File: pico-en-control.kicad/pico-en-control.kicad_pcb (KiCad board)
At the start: 2 copper layers, 17 parts, among them J1 JST-PH2 Bat, J2 Pico Pin 1-7, J3 Pico Pin 40-34, SW1 SW_Push, U1 SN74HC74N, U2 PCF8563T, Y1 Crystal

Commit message: draft routing
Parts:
- moved D1 15.8 mm to (103.3, 104.5)
- moved R1 14.7 mm to (115.7, 115.7), turned to 90 degrees
- moved SW1 14.2 mm to (113.5, 130.7), turned to 90 degrees
- moved J1 14.1 mm to (106.4, 126.9)
- moved C1 11.6 mm to (106.4, 111.4), turned to 0 degrees
- moved U1 11.1 mm to (109.7, 115.7), turned to 90 degrees
- moved JP1 9.63 mm to (115.2, 112.1), turned to 90 degrees
- moved R5 9.61 mm to (111.4, 109.9), turned to -90 degrees
- moved C3 8.32 mm to (114.1, 102.3), turned to 90 degrees
- moved Y1 8.27 mm to (111.9, 100.1), turned to 180 degrees
- moved C2 8.23 mm to (114.0, 107.9), turned to 90 degrees
- moved R4 6.82 mm to (108.0, 110.0), turned to -90 degrees
- moved R2 6.41 mm to (105.8, 120.5), turned to -90 degrees
- moved R3 6.15 mm to (110.1, 109.9)
- moved U2 2.48 mm to (110.7, 105.1), turned to -90 degrees
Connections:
- J2 pad 2: /GP2 -> unconnected-(J2-Pad2)
- J2 pad 6: /GP4_DONE -> /GP4_CLKOUT
- J2 pad 7: unconnected-(J2-Pad7) -> /GP5_DONE
- JP1 pad 1: /GP2 -> /GP4_CLKOUT
- R1 pad 2: /GP4_DONE -> /GP5_DONE
- R5 pad 1: +BATT -> /CLKOUT
- R5 pad 2: /CLKOUT -> +3V3
- U1 pad 3: /GP4_DONE -> /GP5_DONE
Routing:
- net +BATT: track 0.00 -> 50.6 mm, vias 0 -> 2
- net /1~{PRE}: track 0.00 -> 50.0 mm, vias 0 -> 3
- net /3V3_EN: track 0.00 -> 24.5 mm, vias 0 -> 1
- net /GP5_DONE: track 0.00 -> 13.2 mm, vias 0 -> 1
- net +3V3: track 0.00 -> 12.4 mm, vias 0 -> 1
- net /SDA: track 0.00 -> 12.2 mm, vias 0 -> 1
- net /SCL: track 0.00 -> 12.1 mm, vias 0 -> 1
- net Net-(U1-Pad2): track 0.00 -> 9.89 mm
- net /CLKOUT: track 0.00 -> 6.74 mm, vias 0 -> 1
- net Net-(C3-Pad2): track 0.00 -> 4.57 mm
- net /VSYS: track 0.00 -> 2.98 mm
- net Net-(U2-Pad2): track 0.00 -> 2.80 mm
- net /GP4_CLKOUT: track 0.00 -> 2.27 mm
- net GND: vias 0 -> 1
- added copper zone on B.Cu, net GND
- added copper zone on F.Cu, net GND
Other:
- board outline added: 21 x 33.8 mm

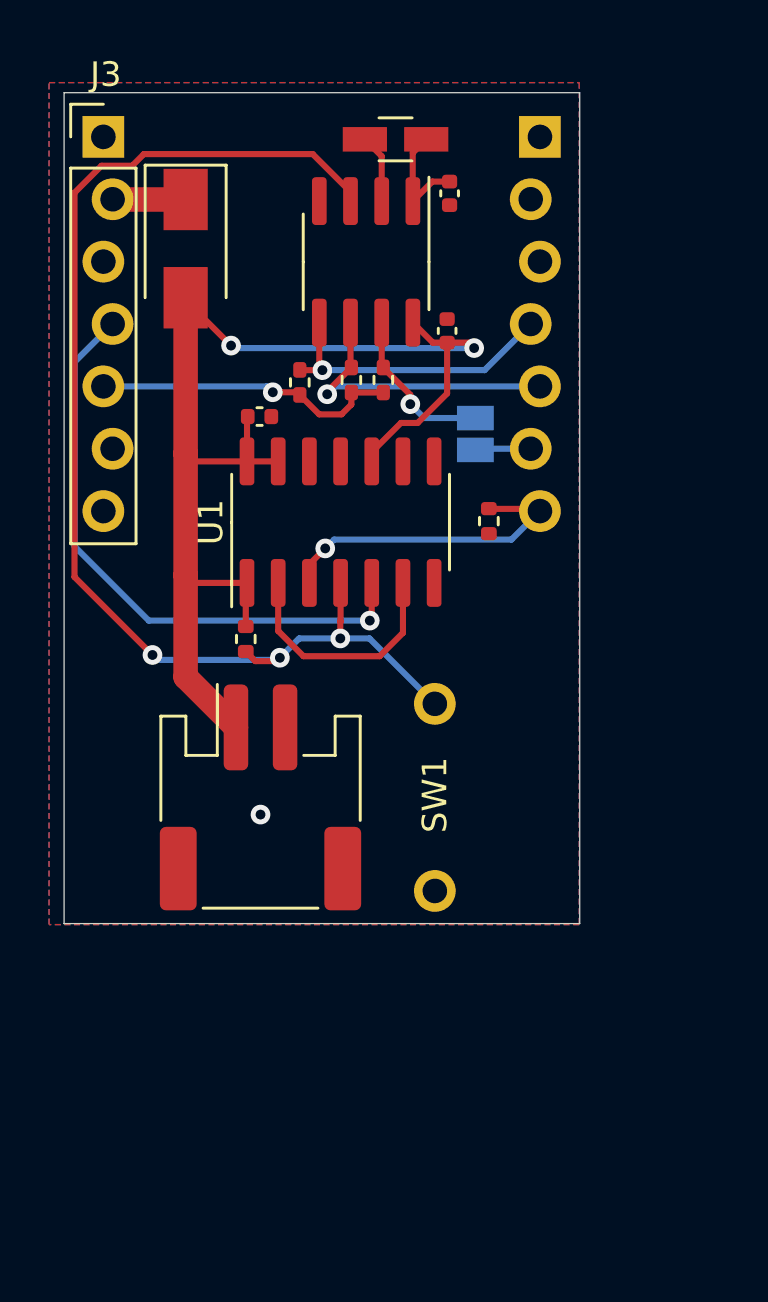
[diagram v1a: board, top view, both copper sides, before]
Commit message: switched to 13-pin connectors
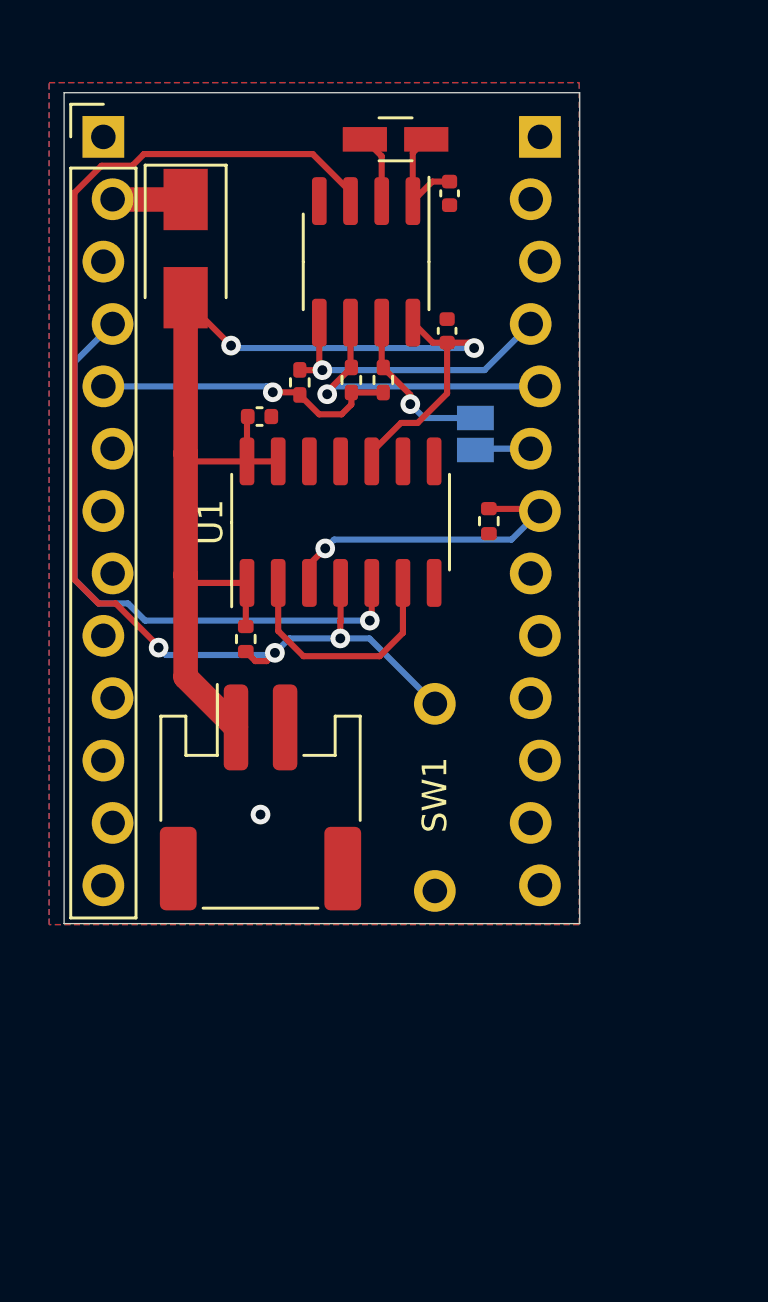
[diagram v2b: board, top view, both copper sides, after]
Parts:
- J2: value Pico Pin 1-7 -> Pico Pin 1-13; footprint user:Connector_1x7_no_solder -> user:Connector_1x13_no_solder; moved to B.Cu
- J3: value Pico Pin 40-34 -> Pico Pin 40-28; footprint user:Connector_1x7_no_solder -> user:Connector_1x13_no_solder
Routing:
- net /3V3_EN: track 24.5 -> 25.3 mm

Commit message: DRC ok
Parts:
- moved C1 2.67 mm to (104.5, 113.3), turned to -90 degrees
- moved R3 0.50 mm to (110.1, 110.4)
- moved R4 0.50 mm to (108.0, 110.5)
- moved R5 0.50 mm to (111.4, 110.4)
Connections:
- J2 pad 13: unconnected-(J2-Pad13) -> GND
- J2 pad 8: unconnected-(J2-Pad8) -> GND
- J3 pad 13: unconnected-(J3-Pad13) -> GND
- J3 pad 8: unconnected-(J3-Pad8) -> GND
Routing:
- net GND: track 0.00 -> 27.7 mm, vias 1 -> 5
- net /SDA: track 12.2 -> 13.0 mm
- net /SCL: track 12.1 -> 12.7 mm

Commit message: Rev2
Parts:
- SW1: value SW_Push -> SW_Push_SLIM
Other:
- board text added: "GND"
- board text added: "GP4_CLKOUT"
- board text added: "GP5_DONE"
- board text added: "On"
- board text added: "SCL"
- board text added: "SDA"
- board text added: "github.com/bablokb/pico-en-control Rev. 2"
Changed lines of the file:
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@@
     )
-  )
-  (footprint "user:SW_PUSH_SLIM_1x4" (layer "F.Cu")
-    (at 113.5 130.71 90)
-    (descr "Prototyping Area")
-    (tags "connector")
-    (property "Sheetfile" "pico-en-control.kicad_sch")
-    (property "Sheetname" "")
-    (attr exclude_from_pos_files)
-    (fp_text reference "SW1" (at 3.91 0 90) (layer "F.SilkS")
-      (effects (font (size 1 1) (thickness 0.15)))
-    )
-    (fp_text value "SW_Push" (at 3.73126 2.92608 90) (layer "F.Fab")
-      (effects (font (size 1 1) (thickness 0.15)))
-    )
-    (fp_text user "${REFERENCE}" (at 1.27 1.27 90) (layer "F.Fab")
-      (effects (font (size 1 1) (thickness 0.15)))
-    )
-    (fp_line (start -1.27 -1.8) (end -1.27 1.8) (layer "F.CrtYd") (width 0.05))
-    (fp_line (start 8.89 -1.8) (end 8.89 1.8) (layer "F.CrtYd") (width 0.05))
-    (fp_line (start -1.27 1.8) (end 8.89 1.8) (layer "F.CrtYd") (width 0.05))
-    (fp_line (start -1.27 -1.8) (end 8.89 -1.8) (layer "F.CrtYd") (width 0.05))
-    (pad "1" thru_hole circle locked (at 0 0 90) (size 1.7 1.7) (drill 1) (layers *.Cu *.Mask)
-      (net 2 "GND") (pinfunction "1") (pintype "passive"))
-    (pad "2" thru_hole circle locked (at 7.62 0 90) (size 1.7 1.7) (drill 1) (layers *.Cu *.Mask)
-      (net 17 "/1~{PRE}") (pinfunction "2") (pintype "passive"))
   )
   (footprint "Crystal:Crystal_SMD_3215-2Pin_3.2x1.5mm" (layer "F.Cu")
@@
     (property "Status" "Active")
     (attr smd)
-    (fp_text reference "U1" (at 0 -5.28 90) (layer "F.SilkS")
+    (fp_text reference "U1" (at 0 -5.28 90) (layer "F.SilkS") hide
       (effects (font (size 1 1) (thickness 0.15)))
     )
@@
     )
   )
+  (footprint "user:SW_PUSH_SLIM_1x4" (layer "F.Cu")
+    (at 113.5 130.7 90)
+    (descr "Slim Pushbutton")
+    (tags "connector")
+    (property "Sheetfile" "pico-en-control.kicad_sch")
+    (property "Sheetname" "")
+    (attr exclude_from_pos_files exclude_from_bom)
+    (fp_text reference "SW1" (at 2.7 0 180) (layer "F.SilkS") hide
+      (effects (font (size 1 1) (thickness 0.15)))
+    )
+    (fp_text value "SW_Push_SLIM" (at 3.73126 2.92608 90) (layer "F.Fab")
+      (effects (font (size 1 1) (thickness 0.15)))
+    )
+    (fp_text user "${REFERENCE}" (at 1.27 1.27 90) (layer "F.Fab")
+      (effects (font (size 1 1) (thickness 0.15)))
+    )
+    (fp_line (start -1.27 1.8) (end 8.89 1.8) (layer "F.CrtYd") (width 0.05))
+    (fp_line (start -1.27 -1.8) (end 8.89 -1.8) (layer "F.CrtYd") (width 0.05))
+    (fp_line (start 8.89 -1.8) (end 8.89 1.8) (layer "F.CrtYd") (width 0.05))
+    (fp_line (start -1.27 -1.8) (end -1.27 1.8) (layer "F.CrtYd") (width 0.05))
+    (pad "1" thru_hole circle (at 0 0 90) (size 1.7 1.7) (drill 1) (layers *.Cu *.Mask)
+      (net 2 "GND") (pinfunction "1") (pintype "passive"))
+    (pad "2" thru_hole circle (at 7.62 0 90) (size 1.7 1.7) (drill 1) (layers *.Cu *.Mask)
+      (net 17 "/1~{PRE}") (pinfunction "2") (pintype "passive"))
+    (pad "3" thru_hole circle (at 5.08 0 90) (size 1.7 1.7) (drill 1) (layers *.Cu *.Mask)
+      (net 2 "GND") (pinfunction "1") (pintype "passive"))
+  )
   (footprint "Resistor_SMD:R_0402_1005Metric" (layer "F.Cu")
     (at 111.4 110.4 -90)
@@
     (property "Sheetfile" "pico-en-control.kicad_sch")
     (property "Sheetname" "")
-    (attr through_hole)
+    (attr through_hole exclude_from_pos_files exclude_from_bom)
     (fp_text reference "J3" (at 0.1 -2.54) (layer "F.SilkS") hide
       (effects (font (size 1 1) (thickness 0.15)))
@@
     (property "Sheetfile" "pico-en-control.kicad_sch")
     (property "Sheetname" "")
-    (attr smd)
+    (attr smd exclude_from_pos_files exclude_from_bom)
     (fp_text reference "J1" (at 0 -5.8) (layer "F.SilkS") hide
       (effects (font (size 1 1) (thickness 0.15)))
@@
     (pad "2" smd roundrect (at 1 -2.85) (size 1 3.5) (layers "F.Cu" "F.Paste" "F.Mask") (roundrect_rratio 0.25)
       (net 2 "GND") (pinfunction "Pin_2") (pintype "passive"))
-    (pad "MP" smd roundrect (at -3.35 2.9) (size 1.5 3.4) (layers "F.Cu" "F.Paste" "F.Mask") (roundrect_rratio 0.166667))
-    (pad "MP" smd roundrect (at 3.35 2.9) (size 1.5 3.4) (layers "F.Cu" "F.Paste" "F.Mask") (roundrect_rratio 0.166667))
+    (pad "MP" smd roundrect (at -3.35 2.9) (size 1.5 3.4) (layers "F.Cu" "F.Paste" "F.Mask") (roundrect_rratio 0.1666673333))
+    (pad "MP" smd roundrect (at 3.35 2.9) (size 1.5 3.4) (layers "F.Cu" "F.Paste" "F.Mask") (roundrect_rratio 0.1666673333))
     (model "${KICAD6_3DMODEL_DIR}/Connector_JST.3dshapes/JST_PH_S2B-PH-SM4-TB_1x02-1MP_P2.00mm_Horizontal.wrl"
       (offset (xyz 0 0 0))
@@
     (property "Sheetfile" "pico-en-control.kicad_sch")
     (property "Sheetname" "")
-    (attr through_hole)
+    (attr through_hole exclude_from_pos_files exclude_from_bom)
     (fp_text reference "J2" (at 0.1 2.54) (layer "B.SilkS") hide
       (effects (font (size 1 1) (thickness 0.15)) (justify mirror))
@@
     (property "Sheetfile" "pico-en-control.kicad_sch")
     (property "Sheetname" "")
-    (attr exclude_from_pos_files)
+    (attr exclude_from_pos_files exclude_from_bom)
     (fp_text reference "JP1" (at 0 1.8 90) (layer "B.SilkS") hide
       (effects (font (size 1 1) (thickness 0.15)) (justify mirror))
@@
       (net 16 "/CLKOUT") (pinfunction "B") (pintype "passive"))
   )
+  (gr_circle (center 104.723607 118.1) (end 104.947214 118.1) (layer "F.SilkS") (width 0.12) (fill solid))
+  (gr_circle (center 114.1 103.6) (end 114.323607 103.6) (layer "F.SilkS") (width 0.12) (fill solid))
   (gr_rect (start 98.4 98.2) (end 119.4 132.04) (layer "Edge.Cuts") (width 0.05) (fill none))
+  (gr_text "GP4_CLKOUT" (at 109.2 112.9) (layer "B.SilkS")
+    (effects (font (size 1 1) (thickness 0.15)) (justify mirror))
+  )
+  (gr_text "GND" (at 112.3 130.8) (layer "B.SilkS")
+    (effects (font (size 1 1) (thickness 0.15)) (justify left mirror))
+  )
+  (gr_text "GND" (at 104.7 130.6) (layer "B.SilkS")
+    (effects (font (size 1 1) (thickness 0.15)) (justify left mirror))
+  )
+  (gr_text "SCL" (at 116.4 109.8) (layer "B.SilkS")
+    (effects (font (size 1 1) (thickness 0.15)) (justify left mirror))
+  )
+  (gr_text "github.com/bablokb/pico-en-control\nRev. 2" (at 103.2 98.5 90) (layer "B.SilkS")
+    (effects (font (size 1 1) (thickness 0.15)) (justify left mirror))
+  )
+  (gr_text "GND" (at 112.4 125.7) (layer "B.SilkS")
+    (effects (font (size 1 1) (thickness 0.15)) (justify left mirror))
+  )
+  (gr_text "SDA" (at 116.3 107.6) (layer "B.SilkS")
+    (effects (font (size 1 1) (thickness 0.15)) (justify left mirror))
+  )
+  (gr_text "GND" (at 116.2 105.2) (layer "B.SilkS")
+    (effects (font (size 1 1) (thickness 0.15)) (justify left mirror))
+  )
+  (gr_text "GP5_DONE" (at 112.5 115.3) (layer "B.SilkS")
+    (effects (font (size 1 1) (thickness 0.15)) (justify mirror))
+  )
+  (gr_text "GND" (at 116 117.9) (layer "B.SilkS")
+    (effects (font (size 1 1) (thickness 0.15)) (justify left mirror))
+  )
+  (gr_text "On" (at 111.3 123.1) (layer "B.SilkS")
+    (effects (font (size 1 1) (thickness 0.15)) (justify mirror))
+  )
+  (gr_text "On" (at 113.5 121.1) (layer "F.SilkS")
+    (effects (font (size 1 1) (thickness 0.15)))
+  )
   (segment (start 105.8 119.94) (end 105.8 118.215) (width 0.25) (layer "F.Cu") (net 1))
   (segment (start 104.52 112.8) (end 104.5 112.82) (width 0.25) (layer "F.Cu") (net 1))

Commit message: Rev3
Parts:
- added J4: Alt-Bat, Connector_PinHeader_2.54mm:PinHeader_1x02_P2.54mm_Vertical, B.Cu at (105.1, 127.4)
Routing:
- net +BATT: track 50.1 -> 53.6 mm
- net GND: vias 5 -> 4
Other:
- board text added: "+"
- board text added: "-"
- board text added: "github.com/bablokb/pico-en-control Rev. 3"
- board text removed: "github.com/bablokb/pico-en-control Rev. 2"
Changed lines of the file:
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@@
       (net 16 "/CLKOUT") (pinfunction "B") (pintype "passive"))
+  )
+  (footprint "Connector_PinHeader_2.54mm:PinHeader_1x02_P2.54mm_Vertical" (layer "B.Cu")
+    (at 105.1 127.4 -90)
+    (descr "Through hole straight pin header, 1x02, 2.54mm pitch, single row")
+    (tags "Through hole pin header THT 1x02 2.54mm single row")
+    (property "Sheetfile" "pico-en-control.kicad_sch")
+    (property "Sheetname" "")
+    (attr through_hole exclude_from_pos_files exclude_from_bom)
+    (fp_text reference "J4" (at 0 2.33 90) (layer "B.SilkS") hide
+      (effects (font (size 1 1) (thickness 0.15)) (justify mirror))
+    )
+    (fp_text value "Alt-Bat" (at 0 -4.87 90) (layer "B.Fab")
+      (effects (font (size 1 1) (thickness 0.15)) (justify mirror))
+    )
+    (fp_text user "${REFERENCE}" (at 0 -1.27) (layer "B.Fab") hide
+      (effects (font (size 1 1) (thickness 0.15)) (justify mirror))
+    )
+    (fp_line (start -1.33 0) (end -1.33 1.33) (layer "B.SilkS") (width 0.12))
+    (fp_line (start -1.33 -1.27) (end -1.33 -3.87) (layer "B.SilkS") (width 0.12))
+    (fp_line (start 1.33 -1.27) (end 1.33 -3.87) (layer "B.SilkS") (width 0.12))
+    (fp_line (start -1.33 1.33) (end 0 1.33) (layer "B.SilkS") (width 0.12))
+    (fp_line (start -1.33 -3.87) (end 1.33 -3.87) (layer "B.SilkS") (width 0.12))
+    (fp_line (start -1.33 -1.27) (end 1.33 -1.27) (layer "B.SilkS") (width 0.12))
+    (fp_line (start -1.8 -4.35) (end 1.8 -4.35) (layer "B.CrtYd") (width 0.05))
+    (fp_line (start 1.8 1.8) (end -1.8 1.8) (layer "B.CrtYd") (width 0.05))
+    (fp_line (start -1.8 1.8) (end -1.8 -4.35) (layer "B.CrtYd") (width 0.05))
+    (fp_line (start 1.8 -4.35) (end 1.8 1.8) (layer "B.CrtYd") (width 0.05))
+    (fp_line (start 1.27 -3.81) (end -1.27 -3.81) (layer "B.Fab") (width 0.1))
+    (fp_line (start 1.27 1.27) (end 1.27 -3.81) (layer "B.Fab") (width 0.1))
+    (fp_line (start -0.635 1.27) (end 1.27 1.27) (layer "B.Fab") (width 0.1))
+    (fp_line (start -1.27 0.635) (end -0.635 1.27) (layer "B.Fab") (width 0.1))
+    (fp_line (start -1.27 -3.81) (end -1.27 0.635) (layer "B.Fab") (width 0.1))
+    (pad "1" thru_hole rect (at 0 0 270) (size 1.7 1.7) (drill 1) (layers *.Cu *.Mask)
+      (net 1 "+BATT") (pinfunction "Pin_1") (pintype "passive"))
+    (pad "2" thru_hole oval (at 0 -2.54 270) (size 1.7 1.7) (drill 1) (layers *.Cu *.Mask)
+      (net 2 "GND") (pinfunction "Pin_2") (pintype "passive"))
+    (model "${KICAD6_3DMODEL_DIR}/Connector_PinHeader_2.54mm.3dshapes/PinHeader_1x02_P2.54mm_Vertical.wrl"
+      (offset (xyz 0 0 0))
+      (scale (xyz 1 1 1))
+      (rotate (xyz 0 0 0))
+    )
   )
   (gr_circle (center 104.723607 118.1) (end 104.947214 118.1) (layer "F.SilkS") (width 0.12) (fill solid))
@@
     (effects (font (size 1 1) (thickness 0.15)) (justify left mirror))
   )
-  (gr_text "github.com/bablokb/pico-en-control\nRev. 2" (at 103.2 98.5 90) (layer "B.SilkS")
+  (gr_text "github.com/bablokb/pico-en-control\nRev. 3" (at 103.2 98.5 90) (layer "B.SilkS")
     (effects (font (size 1 1) (thickness 0.15)) (justify left mirror))
+  )
+  (gr_text "-" (at 107.6 129.2 180) (layer "B.SilkS")
+    (effects (font (size 1 1) (thickness 0.15)) (justify mirror))
   )
   (gr_text "GND" (at 112.4 125.7) (layer "B.SilkS")
@@
   (gr_text "SDA" (at 116.3 107.6) (layer "B.SilkS")
     (effects (font (size 1 1) (thickness 0.15)) (justify left mirror))
+  )
+  (gr_text "+" (at 105.2 129.2 180) (layer "B.SilkS")
+    (effects (font (size 1 1) (thickness 0.15)) (justify mirror))
   )
   (gr_text "GND" (at 116.2 105.2) (layer "B.SilkS")
@@
   (gr_text "On" (at 111.3 123.1) (layer "B.SilkS")
     (effects (font (size 1 1) (thickness 0.15)) (justify mirror))
+  )
+  (gr_text "+" (at 105.2 129.1) (layer "F.SilkS")
+    (effects (font (size 1 1) (thickness 0.15)))
+  )
+  (gr_text "-" (at 107.6 129.1) (layer "F.SilkS")
+    (effects (font (size 1 1) (thickness 0.15)))
   )
   (gr_text "On" (at 113.5 121.1) (layer "F.SilkS")
@@
   (segment (start 105.2 108.5) (end 103.35 106.65) (width 0.25) (layer "F.Cu") (net 1))
   (segment (start 105.435 112.8) (end 104.52 112.8) (width 0.25) (layer "F.Cu") (net 1))
+  (segment (start 105.4 124.05) (end 105.4 127.1) (width 1) (layer "F.Cu") (net 1))
   (segment (start 112.605 107.565) (end 113.42 108.38) (width 0.25) (layer "F.Cu") (net 1))
   (segment (start 105.85 118.165) (end 103.665 118.165) (width 0.25) (layer "F.Cu") (net 1))
   (segment (start 103.35 122) (end 103.35 117.85) (width 1) (layer "F.Cu") (net 1))
+  (segment (start 105.4 127.1) (end 105.1 127.4) (width 1) (layer "F.Cu") (net 1))
   (segment (start 105.8 118.215) (end 105.85 118.165) (width 0.25) (layer "F.Cu") (net 1))
   (segment (start 103.35 106.65) (end 103.35 106.55) (width 0.25) (layer "F.Cu") (net 1))
@@
   (via (at 106.4 102.6) (size 0.8) (drill 0.4) (layers "F.Cu" "B.Cu") (net 2))
   (via (at 105.2 99.3) (size 0.8) (drill 0.4) (layers "F.Cu" "B.Cu") (net 2))
-  (via (at 106.4 127.6) (size 0.8) (drill 0.4) (layers "F.Cu" "B.Cu") (free) (net 2))
   (via (at 115.7 99.4) (size 0.8) (drill 0.4) (layers "F.Cu" "B.Cu") (free) (net 2))
   (via (at 114.1 104.6) (size 0.8) (drill 0.4) (layers "F.Cu" "B.Cu") (free) (net 2))
